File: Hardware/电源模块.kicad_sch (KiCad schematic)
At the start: 28 parts, among them J3 Barrel_Jack_Switch, U2 MP2225GJ, U3 AMS1117-1.8, U4 AMS1117-2.5, U5 AMS1117-3.3

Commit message: nm
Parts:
- removed C10: 33pF, Capacitor_SMD:C_0402_1005Metric, symbol Device:C
- removed C11: 22uF, Capacitor_SMD:C_1206_3216Metric, symbol Device:C
- removed C12, C13, C14, C18, C19, C20: 10uF, Capacitor_SMD:C_0603_1608Metric, symbol Device:C
- removed C15, C16, C17, C21, C22, C23, C7, C8, C9: 104, Capacitor_SMD:C_0402_1005Metric, symbol Device:C
- removed C6: 22uF, Capacitor_SMD:C_1210_3225Metric, symbol Device:C
- removed L1: 4.7uH, Inductor_SMD:L_Chilisin_BMRx00060630, symbol Device:L
- removed R6: 100K, Resistor_SMD:R_0402_1005Metric, symbol Device:R
- removed R7: 40.2K, Resistor_SMD:R_0402_1005Metric, symbol Device:R
- removed R8: 5.49K, Resistor_SMD:R_0402_1005Metric, symbol Device:R
- removed U3: AMS1117-1.8, Package_TO_SOT_SMD:SOT-223-3_TabPin2, symbol Regulator_Linear:AMS1117-1.8
- removed U4: AMS1117-2.5, Package_TO_SOT_SMD:SOT-223-3_TabPin2, symbol Regulator_Linear:AMS1117-2.5
- removed U5: AMS1117-3.3, Package_TO_SOT_SMD:SOT-223-3_TabPin2, symbol Regulator_Linear:AMS1117-3.3
- added C10, C14, C16, C18, C8, C9: 10uF, Capacitor_SMD:C_0402_1005Metric, symbol Device:C_Small
- added C11, C12, C13: 220pF, Capacitor_SMD:C_0402_1005Metric, symbol Device:C_Small
- added C15: 1uF, Capacitor_SMD:C_0402_1005Metric, symbol Device:C_Small
- added C17, C23: 22uF, Capacitor_SMD:C_0805_2012Metric, symbol Device:C_Small
- added C19, C20, C21: 104, Capacitor_SMD:C_0402_1005Metric, symbol Device:C_Small
- added C22: 33pF, Capacitor_SMD:C_0402_1005Metric, symbol Device:C_Small
- added L1, L2, L3: 1.5uH, Inductor_SMD:L_Chilisin_BMRA00050520, symbol Device:L_Small
- added L4: 4.7uH, Inductor_SMD:L_Chilisin_BMRA00050520, symbol Device:L_Small
- added R10: 200K, Resistor_SMD:R_0402_1005Metric, symbol Device:R_Small
- added R11, R12, R13: 100K, Resistor_SMD:R_0402_1005Metric, symbol Device:R_Small
- added R14: 40.2K, Resistor_SMD:R_0402_1005Metric, symbol Device:R_Small
- added R15: 5.49K, Resistor_SMD:R_0402_1005Metric, symbol Device:R_Small
- added R6: 510K, Resistor_SMD:R_0402_1005Metric, symbol Device:R_Small
- added R7: 110K, Resistor_SMD:R_0402_1005Metric, symbol Device:R_Small
- added R8: 470K, Resistor_SMD:R_0402_1005Metric, symbol Device:R_Small
- added R9: 150K, Resistor_SMD:R_0402_1005Metric, symbol Device:R_Small
- added U2: EA3036C, Package_DFN_QFN:QFN-20-1EP_3x3mm_P0.4mm_EP1.65x1.65mm, symbol Power_Management:EA3036C
- renumbered U2 to U3
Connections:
- net +12V: now also C17.1, C19.1, R13.1
- net +1V8: now also C10.1, C13.1, L3.1, R10.1
- net +2V5: now also C12.1, C9.1, L2.1, R8.1
- net +3V3: now also C11.1, C8.1, L1.1, R6.1
- net +5V: now also C14.1, C15.1, C16.1, C18.1, C22.1, C23.1, L4.2, R12.1, R14.1, U2.10 (VIN1), U2.16 (VCC), U2.19 (VIN3), U2.7 (VIN2)
- net GND: now also C10.2, C14.2, C15.2, C16.2, C17.2, C18.2, C19.2, C20.1, C23.2, C8.2, C9.2, R11.1, R15.2, R7.1, R9.1, U2.1 (GND3), U2.12 (GND1), U2.13 (GND1), U2.15 (AGND), U2.17 (AGND), U2.21 (EP), U2.4 (GND2), U2.5 (GND2)
- net at U3.8 (FB): now also C22.2, R14.2, R15.1
- net at U3.7 (VCC): now also C20.2
- net at U3.3 (SW): now also C21.2, L4.1
- net at U3.6 (EN/SYNC): now also R13.2
- net at U3.5 (BST): now also C21.1
- new net: L3.2, U2.2 (FB3)
- new net: L1.2, U2.11 (LX1)
- new net: C12.2, R8.2, R9.2, U2.3 (FB2)
- new net: C11.2, R6.2, R7.2, U2.14 (FB1)
- new net: R12.2, U2.18 (EN3), U2.8 (EN2), U2.9 (EN1)
- new net: C13.2, R10.2, R11.2, U2.20 (LX3)
- new net: L2.2, U2.6 (LX2)
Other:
- moved on the sheet: J3, SW5, U3

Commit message: nm
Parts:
- J3: footprint Connector_BarrelJack:BarrelJack_CLIFF_FC681465S_SMT_Horizontal -> Connector_BarrelJack:BarrelJack_XKB_DC-044A-2.5A-2.5
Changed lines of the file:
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@@
       (effects (font (size 1.27 1.27)) hide)
     )
-    (property "Footprint" "Connector_BarrelJack:BarrelJack_CLIFF_FC681465S_SMT_Horizontal" (at 137.16 44.196 0)
+    (property "Footprint" "Connector_BarrelJack:BarrelJack_XKB_DC-044A-2.5A-2.5" (at 137.16 44.196 0)
       (effects (font (size 1.27 1.27)) hide)
     )

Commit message: 完成布局
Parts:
- removed J3: Barrel_Jack_Switch, Connector_BarrelJack:BarrelJack_XKB_DC-044A-2.5A-2.5, symbol Connector:Barrel_Jack_Switch
- added J3: Barrel_Jack_Switch_MountingPin, Connector_BarrelJack:BarrelJack_XKB_DC-044A-2.5A-2.5, symbol Connector:Barrel_Jack_Switch_MountingPin
- L1, L2, L3, L4: footprint Inductor_SMD:L_Chilisin_BMRA00050520 -> Inductor_SMD:L_1206_3216Metric
- SW5: footprint Library:SW -> Button_Switch_THT:SW_XKB_SS-12D10L5
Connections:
- net GND: now also J3.2, J3.3, J3.MP (MountPin)
- net at L3.2: now also U2.20 (LX3); no longer U2.2 (FB3)
- net at C13.2, R10.2, R11.2: now also U2.2 (FB3); no longer U2.20 (LX3)
- net at SW5.2: now also J3.1
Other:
- moved on the sheet: SW5
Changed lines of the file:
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@@
   (junction (at 39.37 57.15) (diameter 0) (color 0 0 0 0)
   )
+  (junction (at 146.05 50.8) (diameter 0) (color 0 0 0 0)
+  )
   (junction (at 39.37 21.59) (diameter 0) (color 0 0 0 0)
   )
-  (no_connect (at 152.4 41.91))
+  (no_connect (at 152.4 44.45))
   (wire (pts (xy 133.35 87.63) (xy 135.89 87.63))
     (stroke (width 0) (type default))
@@
     (stroke (width 0) (type default))
   )
-  (wire (pts (xy 156.21 40.64) (xy 156.21 41.91))
+  (wire (pts (xy 156.21 40.64) (xy 156.21 44.45))
     (stroke (width 0) (type default))
   )
@@
     (stroke (width 0) (type default))
   )
+  (wire (pts (xy 146.05 50.8) (xy 146.05 52.07))
+    (stroke (width 0) (type default))
+  )
   (wire (pts (xy 66.04 72.39) (xy 66.04 73.66))
     (stroke (width 0) (type default))
@@
     (stroke (width 0) (type default))
   )
-  (wire (pts (xy 160.02 40.64) (xy 160.02 41.91))
+  (wire (pts (xy 160.02 40.64) (xy 160.02 44.45))
     (stroke (width 0) (type default))
   )
@@
     (stroke (width 0) (type default))
   )
+  (wire (pts (xy 135.89 50.8) (xy 146.05 50.8))
+    (stroke (width 0) (type default))
+  )
   (wire (pts (xy 86.36 44.45) (xy 81.28 44.45))
     (stroke (width 0) (type default))
@@
     (stroke (width 0) (type default))
   )
-  (wire (pts (xy 146.05 45.72) (xy 146.05 46.99))
+  (wire (pts (xy 146.05 45.72) (xy 146.05 50.8))
     (stroke (width 0) (type default))
   )
@@
       (effects (font (size 1.27 1.27)))
     )
-    (property "Footprint" "Inductor_SMD:L_Chilisin_BMRA00050520" (at 44.45 57.15 0)
+    (property "Footprint" "Inductor_SMD:L_1206_3216Metric" (at 44.45 57.15 0)
       (effects (font (size 1.27 1.27)) hide)
     )
@@
     )
   )
-  (symbol (lib_id "power:GND") (at 146.05 46.99 0) (unit 1)
-    (in_bom yes) (on_board yes) (dnp no) (fields_autoplaced)
-    (property "Reference" "#PWR035" (at 146.05 53.34 0)
-      (effects (font (size 1.27 1.27)) hide)
-    )
-    (property "Value" "GND" (at 146.05 52.07 0)
-      (effects (font (size 1.27 1.27)))
-    )
-    (property "Footprint" "" (at 146.05 46.99 0)
-      (effects (font (size 1.27 1.27)) hide)
-    )
-    (property "Datasheet" "" (at 146.05 46.99 0)
+  (symbol (lib_id "power:GND") (at 146.05 52.07 0) (unit 1)
+    (in_bom yes) (on_board yes) (dnp no) (fields_autoplaced)
+    (property "Reference" "#PWR035" (at 146.05 58.42 0)
+      (effects (font (size 1.27 1.27)) hide)
+    )
+    (property "Value" "GND" (at 146.05 57.15 0)
+      (effects (font (size 1.27 1.27)))
+    )
+    (property "Footprint" "" (at 146.05 52.07 0)
+      (effects (font (size 1.27 1.27)) hide)
+    )
+    (property "Datasheet" "" (at 146.05 52.07 0)
       (effects (font (size 1.27 1.27)) hide)
     )
@@
       (effects (font (size 1.27 1.27)))
     )
-    (property "Footprint" "Inductor_SMD:L_Chilisin_BMRA00050520" (at 44.45 21.59 0)
+    (property "Footprint" "Inductor_SMD:L_1206_3216Metric" (at 44.45 21.59 0)
       (effects (font (size 1.27 1.27)) hide)
     )
@@
       (effects (font (size 1.27 1.27)))
     )
-    (property "Footprint" "Inductor_SMD:L_Chilisin_BMRA00050520" (at 44.45 39.37 0)
+    (property "Footprint" "Inductor_SMD:L_1206_3216Metric" (at 44.45 39.37 0)
       (effects (font (size 1.27 1.27)) hide)
     )
@@
     )
   )
+  (symbol (lib_id "Connector:Barrel_Jack_Switch_MountingPin") (at 135.89 43.18 0) (unit 1)
+    (in_bom yes) (on_board yes) (dnp no)
+    (property "Reference" "J3" (at 135.89 36.83 0)
+      (effects (font (size 1.27 1.27)))
+    )
+    (property "Value" "Barrel_Jack_Switch_MountingPin" (at 135.89 38.1 0)
+      (effects (font (size 1.27 1.27)) hide)
+    )
+    (property "Footprint" "Connector_BarrelJack:BarrelJack_XKB_DC-044A-2.5A-2.5" (at 137.16 44.196 0)
+      (effects (font (size 1.27 1.27)) hide)
+    )
+    (property "Datasheet" "~" (at 137.16 44.196 0)
+      (effects (font (size 1.27 1.27)) hide)
+    )
+    (pin "1")
+    (pin "2")
+    (pin "3")
+    (pin "MP")
+    (instances
+      (project "Warehouse-on-STM32"
+        (path "/2599b9a9-6312-402b-9c24-1e87744a4c70/b0fcdae1-8a36-4fea-9ba4-a386ad3e5014"
+          (reference "J3") (unit 1)
+        )
+      )
+    )
+  )
   (symbol (lib_id "Device:R_Small") (at 29.21 62.23 90) (unit 1)
     (in_bom yes) (on_board yes) (dnp no)
@@
       (effects (font (size 1.27 1.27)))
     )
-    (property "Footprint" "Inductor_SMD:L_Chilisin_BMRA00050520" (at 171.45 69.85 0)
+    (property "Footprint" "Inductor_SMD:L_1206_3216Metric" (at 171.45 69.85 0)
       (effects (font (size 1.27 1.27)) hide)
     )
@@
     )
   )
-  (symbol (lib_id "Switch:SW_SLIDE") (at 160.02 50.165 0) (unit 1)
+  (symbol (lib_id "Switch:SW_SLIDE") (at 156.21 48.895 0) (unit 1)
     (in_bom yes) (on_board yes) (dnp no)
-    (property "Reference" "SW5" (at 157.48 49.53 0)
-      (effects (font (size 1.27 1.27)) (justify left))
-    )
-    (property "Value" "~" (at 167.64 46.355 0)
-      (effects (font (size 1.27 1.27)))
-    )
-    (property "Footprint" "Library:SW" (at 167.64 46.355 0)
-      (effects (font (size 1.27 1.27)) hide)
-    )
-    (property "Datasheet" "" (at 167.64 46.355 0)
+    (property "Reference" "SW5" (at 157.48 52.07 0)
+      (effects (font (size 1.27 1.27)) (justify left))
+    )
+    (property "Value" "~" (at 163.83 45.085 0)
+      (effects (font (size 1.27 1.27)))
+    )
+    (property "Footprint" "Button_Switch_THT:SW_XKB_SS-12D10L5" (at 163.83 45.085 0)
+      (effects (font (size 1.27 1.27)) hide)
+    )
+    (property "Datasheet" "" (at 163.83 45.085 0)
       (effects (font (size 1.27 1.27)) hide)
     )
@@
         )
       )
-    )
-  )
-  (symbol (lib_id "Connector:Barrel_Jack_Switch") (at 135.89 43.18 0) (unit 1)
-    (in_bom yes) (on_board yes) (dnp no) (fields_autoplaced)
-    (property "Reference" "J3" (at 135.89 38.1 0)
-      (effects (font (size 1.27 1.27)))
-    )
-    (property "Value" "Barrel_Jack_Switch" (at 135.89 38.1 0)
-      (effects (font (size 1.27 1.27)) hide)
-    )
-    (property "Footprint" "Connector_BarrelJack:BarrelJack_XKB_DC-044A-2.5A-2.5" (at 137.16 44.196 0)
-      (effects (font (size 1.27 1.27)) hide)
-    )
-    (property "Datasheet" "~" (at 137.16 44.196 0)
-      (effects (font (size 1.27 1.27)) hide)
-    )
-    (pin "1")
-    (pin "2")
-    (pin "3")
-    (instances
-      (project "Warehouse-on-STM32"
-        (path "/2599b9a9-6312-402b-9c24-1e87744a4c70/b0fcdae1-8a36-4fea-9ba4-a386ad3e5014"
-          (reference "J3") (unit 1)
-        )
-      )

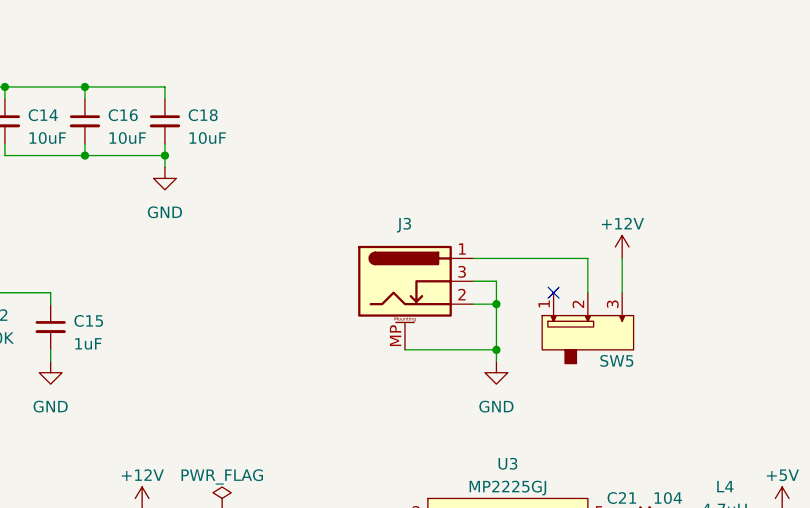
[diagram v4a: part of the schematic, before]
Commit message: 修改了电机驱动芯片旁的电容封装为0603
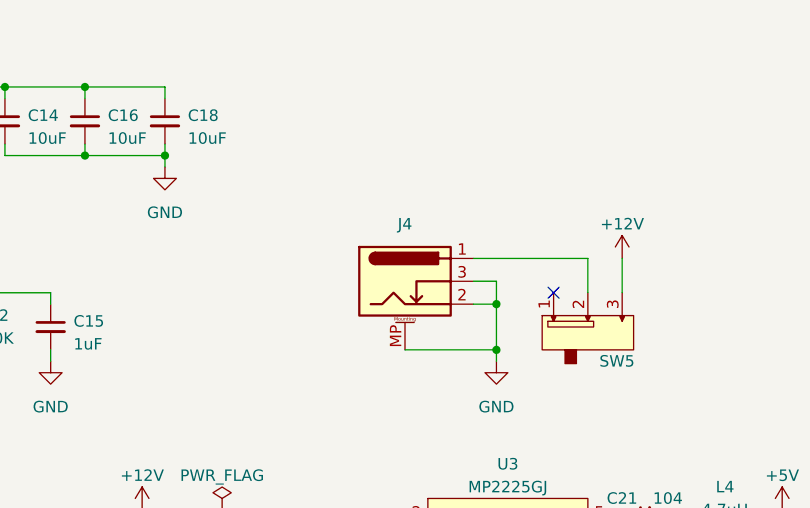
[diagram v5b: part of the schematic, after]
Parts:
- renumbered J3 to J4

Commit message: update
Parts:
- removed C10, C14, C16, C18, C8, C9: 10uF, Capacitor_SMD:C_0402_1005Metric, symbol Device:C_Small
- removed C11, C12, C13: 220pF, Capacitor_SMD:C_0402_1005Metric, symbol Device:C_Small
- removed C15: 1uF, Capacitor_SMD:C_0402_1005Metric, symbol Device:C_Small
- removed L1, L2, L3: 1.5uH, Inductor_SMD:L_1206_3216Metric, symbol Device:L_Small
- removed R10: 200K, Resistor_SMD:R_0402_1005Metric, symbol Device:R_Small
- removed R11, R12: 100K, Resistor_SMD:R_0402_1005Metric, symbol Device:R_Small
- removed R6: 510K, Resistor_SMD:R_0402_1005Metric, symbol Device:R_Small
- removed R7: 110K, Resistor_SMD:R_0402_1005Metric, symbol Device:R_Small
- removed R8: 470K, Resistor_SMD:R_0402_1005Metric, symbol Device:R_Small
- removed R9: 150K, Resistor_SMD:R_0402_1005Metric, symbol Device:R_Small
- removed U2: EA3036C, Package_DFN_QFN:QFN-20-1EP_3x3mm_P0.4mm_EP1.65x1.65mm, symbol Power_Management:EA3036C
- added C31, C33: 10uF, Capacitor_SMD:C_0402_1005Metric, symbol Device:C
- added C32, C34: 104, Capacitor_SMD:C_0402_1005Metric, symbol Device:C
- added U10: AMS1117-3.3, Package_TO_SOT_SMD:SOT-223-3_TabPin2, symbol Regulator_Linear:AMS1117-3.3
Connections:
- net +3V3: now also C33.1, C34.1, U10.2 (VO)
- net +5V: now also C31.1, C32.1, U10.3 (VI)
- net GND: now also C31.2, C32.2, C33.2, C34.2, U10.1 (GND)
